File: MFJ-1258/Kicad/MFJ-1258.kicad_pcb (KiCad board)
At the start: 2 copper layers, 77.8 x 54.3 mm, 19 parts, among them J1 C64-UserPort, J2 Screw_Terminal_01x01, J3 Screw_Terminal_01x01, Q1 2N3906, Q2 2N3906, Q3 2N3906, U1 NE555P

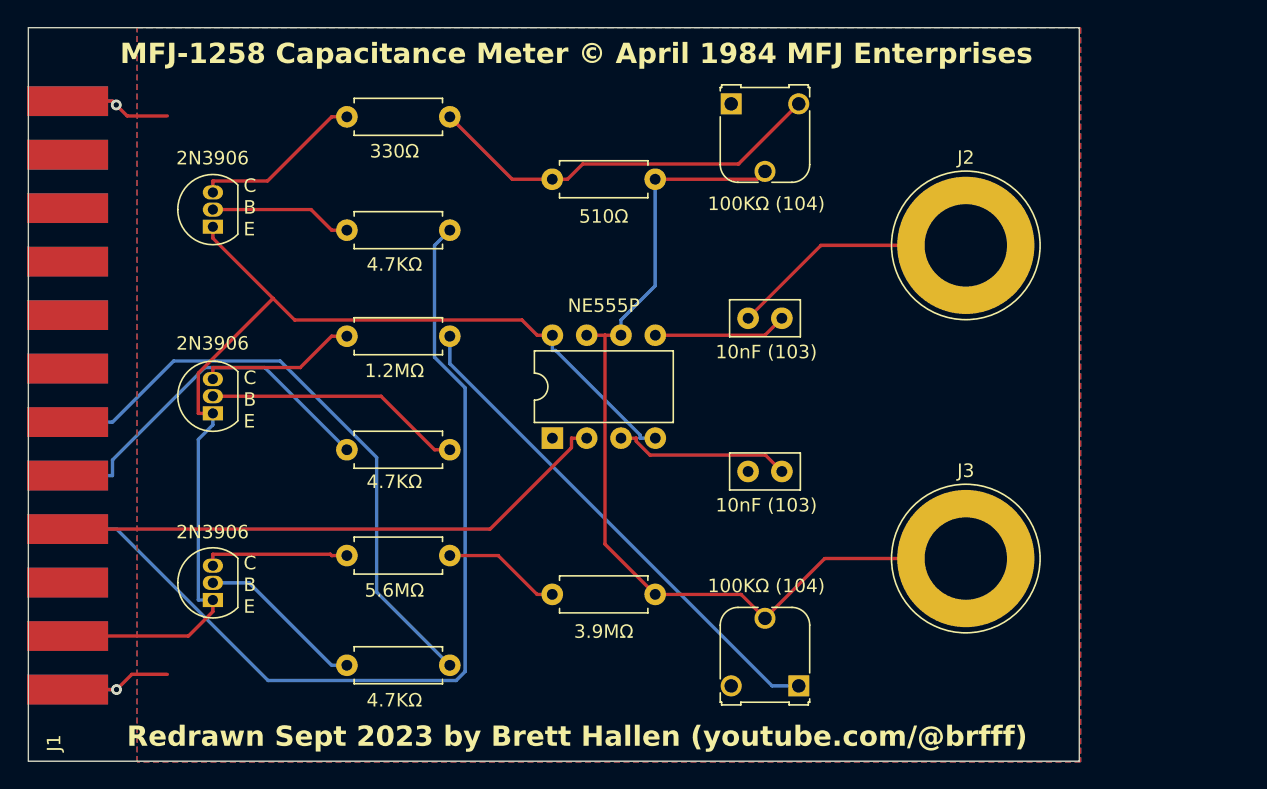
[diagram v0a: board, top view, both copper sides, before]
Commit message: Minor PCB adjustments
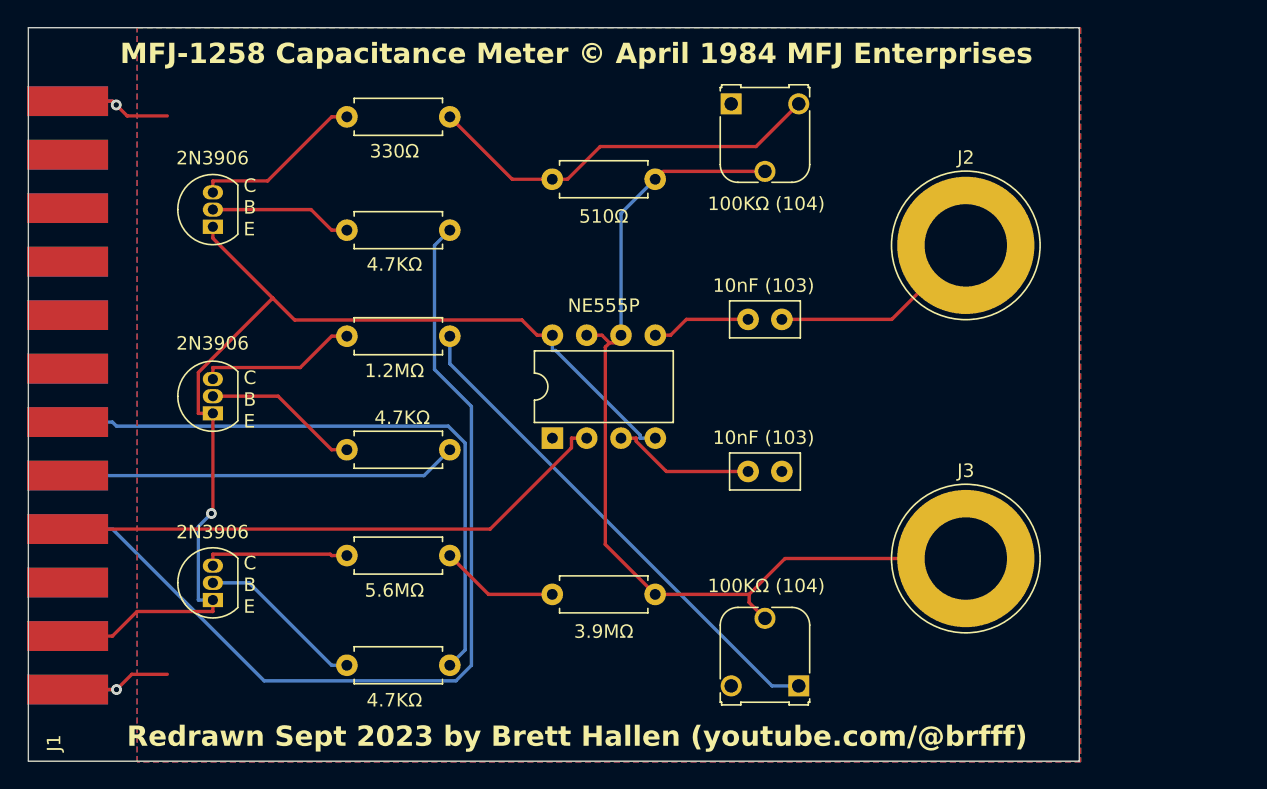
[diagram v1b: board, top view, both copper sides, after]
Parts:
- moved R4 7.62 mm to (118.4, 101.3), turned to 180 degrees
- moved C1 2.50 mm to (143.0, 91.7), turned to 180 degrees
- moved C2 2.50 mm to (143.0, 103.0), turned to 180 degrees
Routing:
- net Net-(Q2-B): track 19.2 -> 11.6 mm
- net Net-(U1-CV): track 9.89 -> 7.35 mm
- net Net-(U1-Q): track 13.1 -> 10.6 mm
- net Net-(J2-Pin_1): track 18.4 -> 15.9 mm
- net /PB2: track 27.2 -> 29.1 mm
- net /PB3: track 45.3 -> 47.0 mm
- net Net-(J3-Pin_1): track 69.8 -> 70.9 mm
- net /+5V: vias 0 -> 1

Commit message: Corrected RV1 value
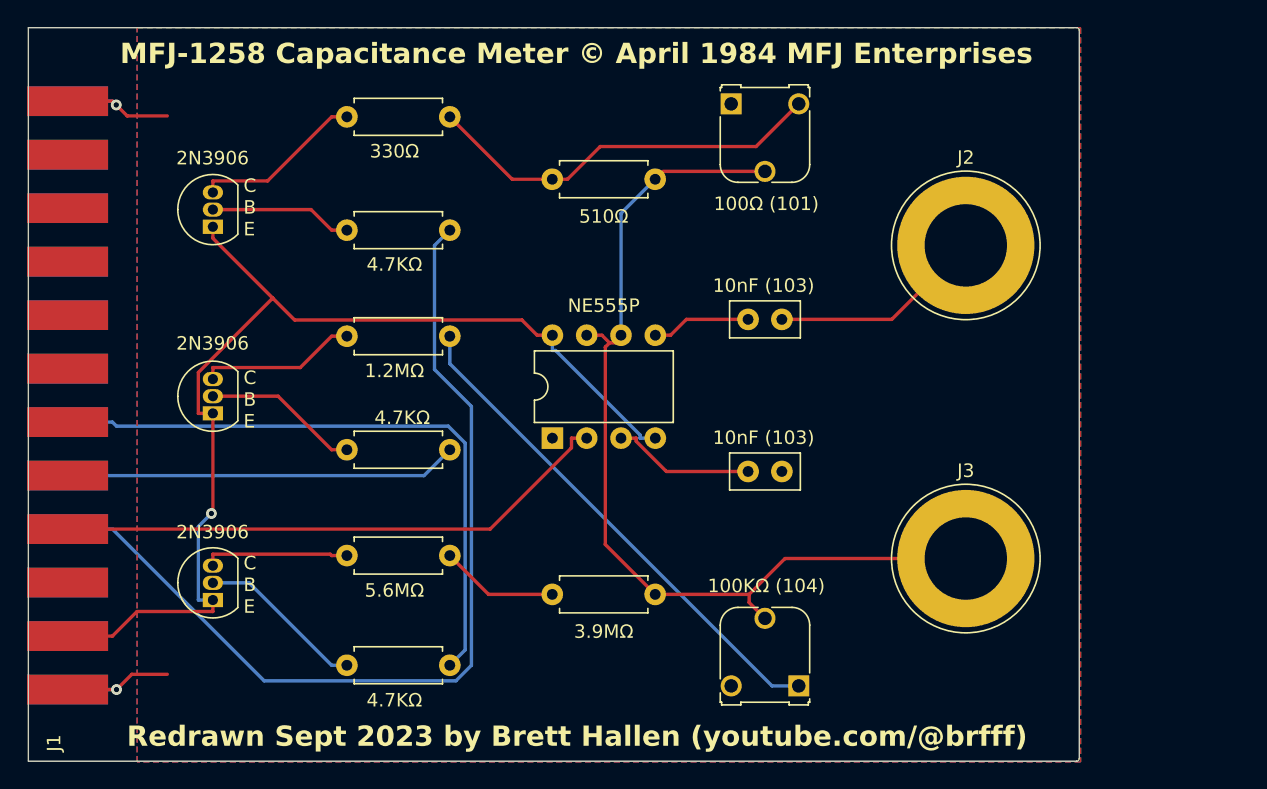
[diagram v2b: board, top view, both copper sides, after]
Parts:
- RV1: value 100KΩ (104) -> 100Ω (101)
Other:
- outline, holes or cut-outs redrawn
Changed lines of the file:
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@@
         (effects (font (size 1 1) (thickness 0.15)))
     )
-    (fp_text value "100KΩ (104)" (at 2.6 7.4) (layer "F.SilkS")
+    (fp_text value "100Ω (101)" (at 2.6 7.4) (layer "F.SilkS")
         (effects (font (size 1 1) (thickness 0.15)))
     )
@@
     )
   )
-  (gr_line (start 87.2 70.1) (end 165 70.1)
+  (gr_arc (start 165 124.2) (mid 164.941421 124.341421) (end 164.8 124.4)
+    (stroke (width 0.1) (type default)) (layer "Edge.Cuts"))
+  (gr_line (start 87.2 70.1) (end 164.8 70.1)
     (stroke (width 0.1) (type default)) (layer "Edge.Cuts"))
   (gr_line (start 87.2 70.1) (end 87.2 124.4)
     (stroke (width 0.1) (type default)) (layer "Edge.Cuts"))
-  (gr_line (start 165 124.4) (end 165 70.1)
+  (gr_arc (start 164.8 70.1) (mid 164.941421 70.158579) (end 165 70.3)
     (stroke (width 0.1) (type default)) (layer "Edge.Cuts"))
-  (gr_line (start 87.2 124.4) (end 165 124.4)
+  (gr_line (start 165 124.2) (end 165 70.3)
+    (stroke (width 0.1) (type default)) (layer "Edge.Cuts"))
+  (gr_line (start 87.2 124.4) (end 164.8 124.4)
     (stroke (width 0.1) (type default)) (layer "Edge.Cuts"))
   (gr_text "MFJ-1258 Capacitance Meter © April 1984 MFJ Enterprises" (at 93.98 72.898) (layer "F.SilkS")

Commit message: Forgot to connect PB7 pin
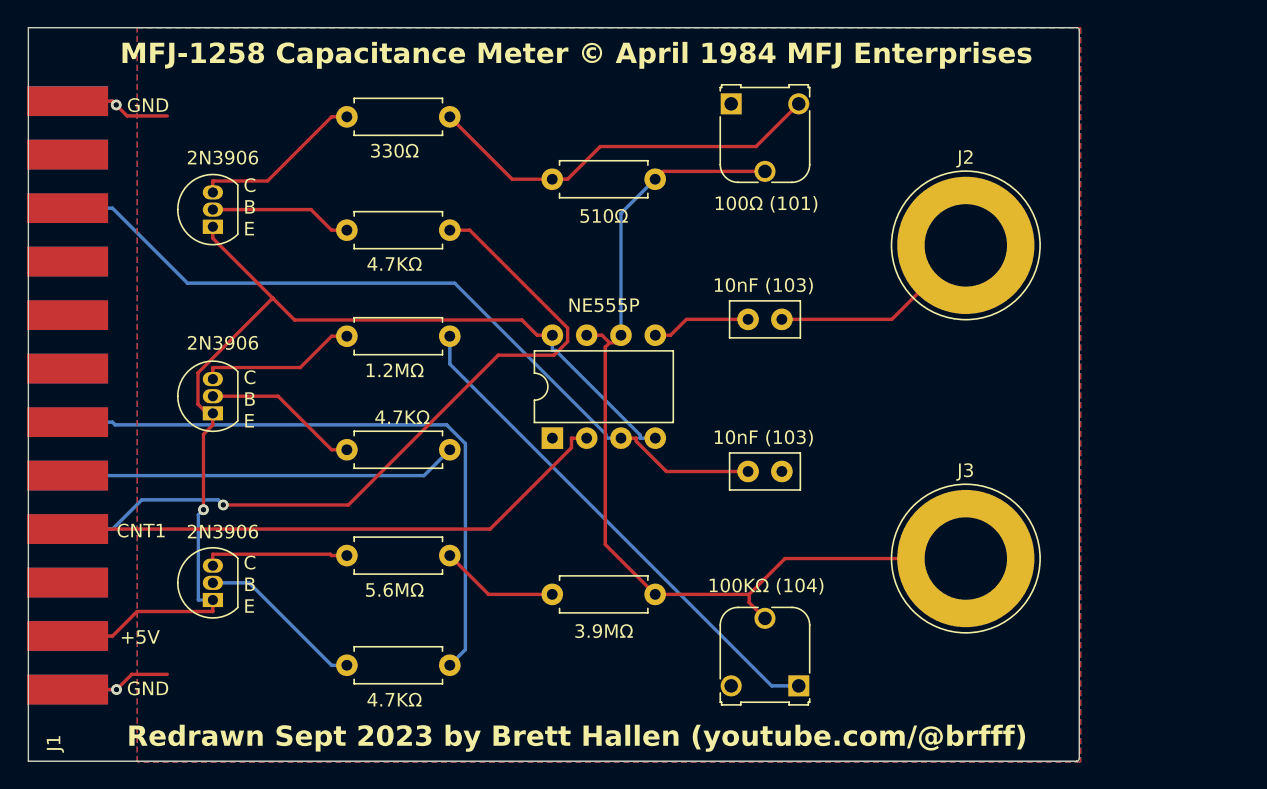
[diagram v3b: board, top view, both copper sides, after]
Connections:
- C2 pad 2: Net-(U1-Q) -> /PB7
- U1 pad 3: Net-(U1-Q) -> /PB7
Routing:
- net /PB7: track 0.00 -> 58.8 mm
- net /PB1: track 68.8 -> 55.8 mm, vias 0 -> 1
- net Net-(U1-Q): track 10.6 -> 0.00 mm
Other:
- board text added: "+5V"
- board text added: "CNT1"
- board text added: "GND"
- board text added: "PB1"
- board text added: "PB2"
- board text added: "PB3"
- board text added: "PB7"
